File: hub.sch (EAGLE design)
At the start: 51 parts, among them U1 LM3526-L, X1 12MHz

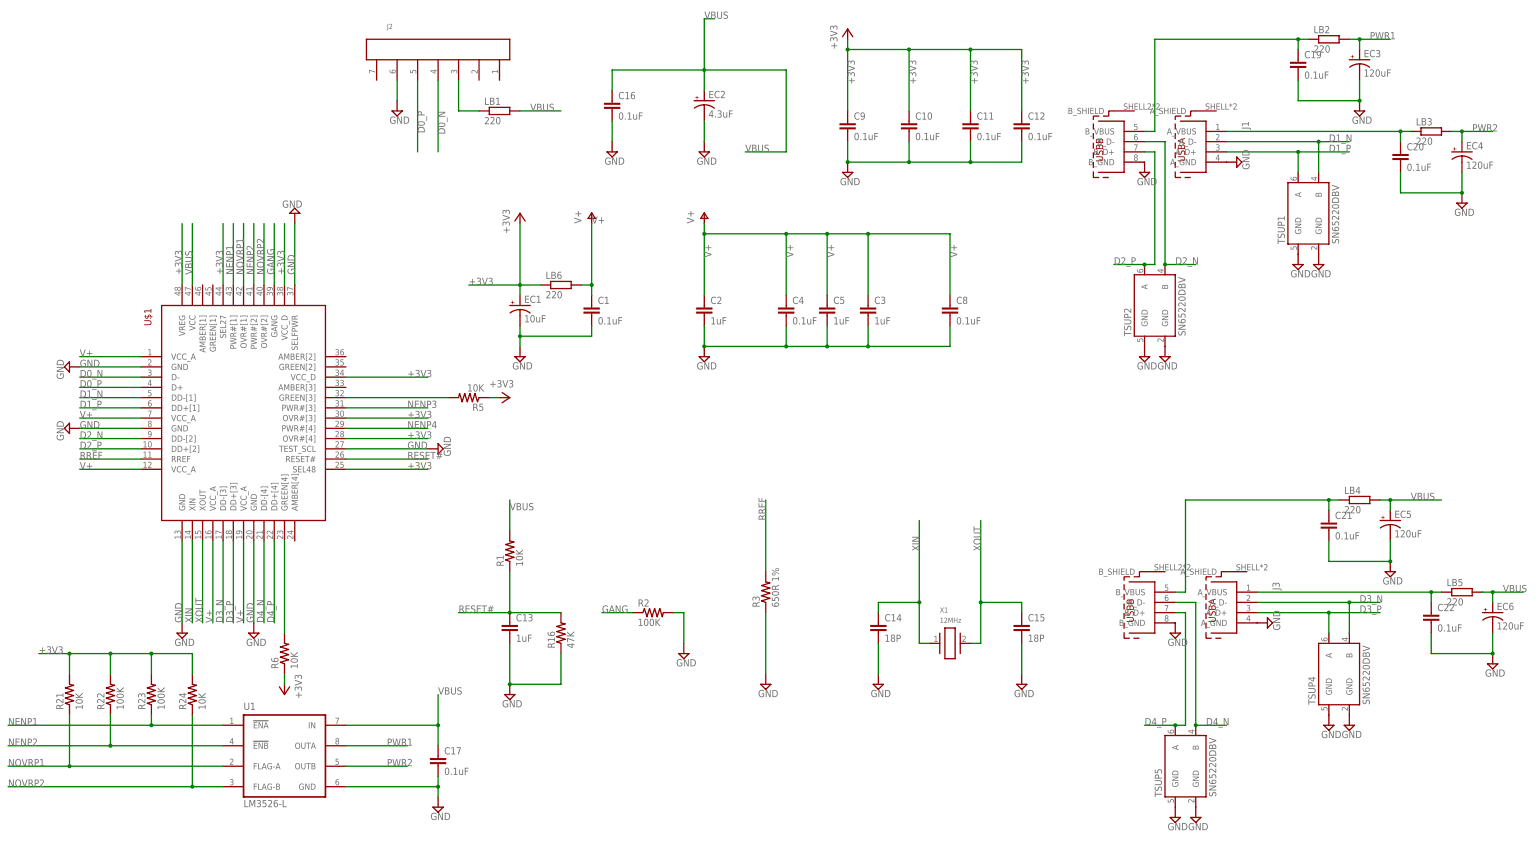
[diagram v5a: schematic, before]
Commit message: finish silk screen
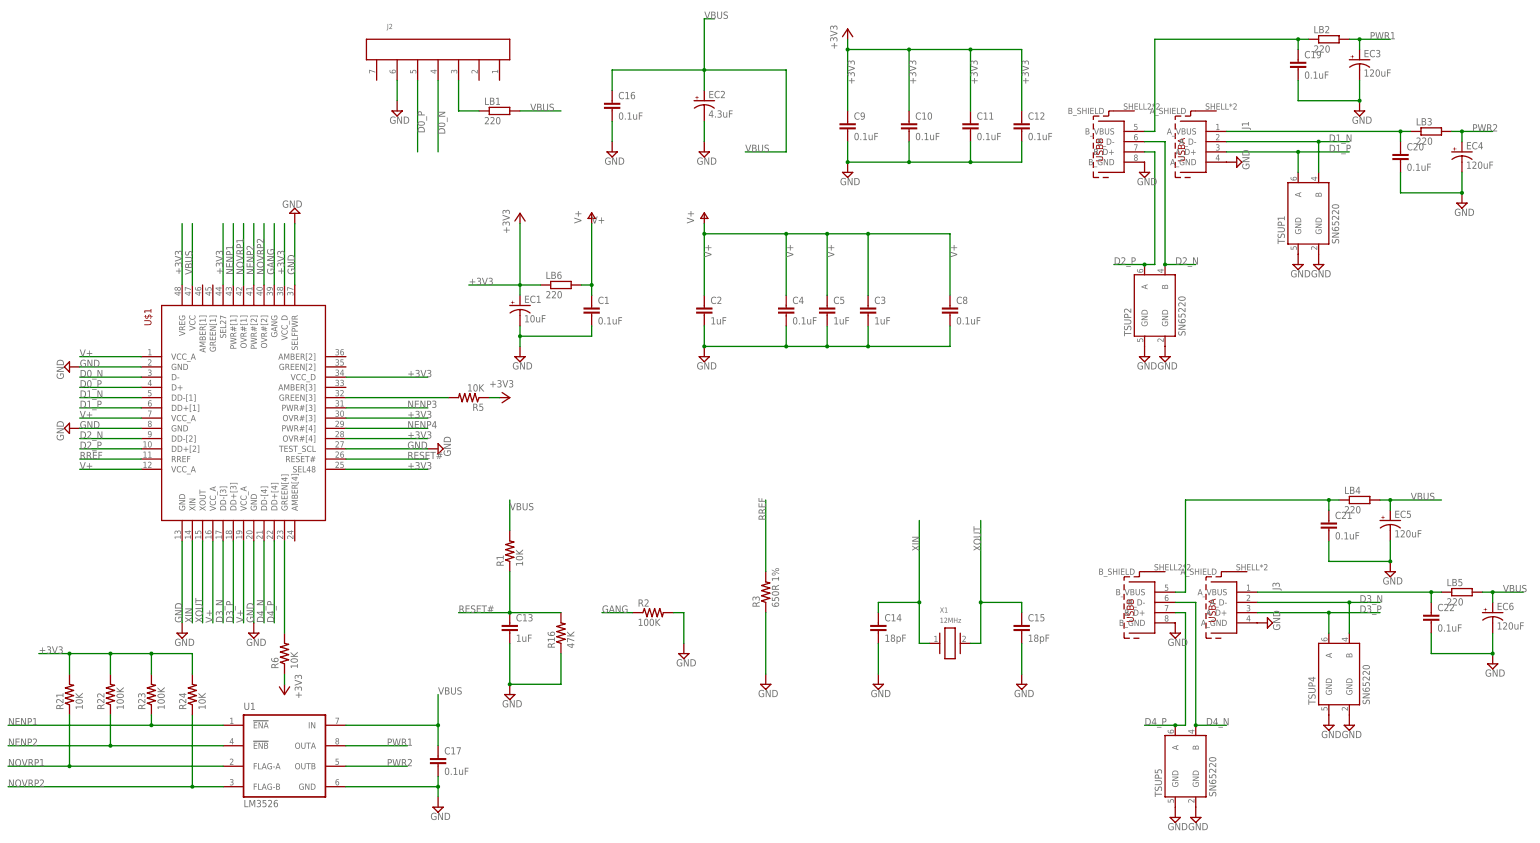
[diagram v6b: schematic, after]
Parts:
- C14, C15: value 18P -> 18pF
- TSUP1, TSUP2, TSUP4, TSUP5: value SN65220DBV -> SN65220
- U$1: value CY7C65634-48AXCT -> CY7C65632; DIGIKEY 428-3153-1-ND -> 428-3155-1-ND; MPN CY7C65634-48AXCT -> CY7C65632-48AXCT; OC_MOUSER 727-CY7C65634-48AXCT -> 727-CY7C65632-48AXCT
- U1: value LM3526-L -> LM3526
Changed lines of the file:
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@@
 <attribute name="OC_MOUSER" value="571-440054-7"/>
 </part>
-<part name="U$1" library="CY7C65634-48AXCT" deviceset="CY7C65634-48AXCT" device="">
-<attribute name="DIGIKEY" value="428-3153-1-ND"/>
-<attribute name="MPN" value="CY7C65634-48AXCT"/>
-<attribute name="OC_MOUSER" value="727-CY7C65634-48AXCT"/>
+<part name="U$1" library="CY7C65634-48AXCT" deviceset="CY7C65634-48AXCT" device="" value="CY7C65632">
+<attribute name="DIGIKEY" value="428-3155-1-ND"/>
+<attribute name="MPN" value="CY7C65632-48AXCT"/>
+<attribute name="OC_MOUSER" value="727-CY7C65632-48AXCT"/>
 </part>
 <part name="SUPPLY1" library="supply2" library_urn="urn:adsk.eagle:library:372" deviceset="GND" device=""/>
@@
 </part>
 <part name="SUPPLY4" library="supply2" library_urn="urn:adsk.eagle:library:372" deviceset="GND" device=""/>
-<part name="C14" library="rcl" library_urn="urn:adsk.eagle:library:334" deviceset="C-EU" device="C0805" package3d_urn="urn:adsk.eagle:package:23617/2" value="18P">
+<part name="C14" library="rcl" library_urn="urn:adsk.eagle:library:334" deviceset="C-EU" device="C0805" package3d_urn="urn:adsk.eagle:package:23617/2" value="18pF">
 <attribute name="DIGIKEY" value="1276-1089-1-ND"/>
 <attribute name="MPN" value="CL10C180JB8NNNC"/>
 <attribute name="OC_MOUSER" value="77-VJ0603A180JXACBC"/>
 </part>
-<part name="C15" library="rcl" library_urn="urn:adsk.eagle:library:334" deviceset="C-EU" device="C0805" package3d_urn="urn:adsk.eagle:package:23617/2" value="18P">
+<part name="C15" library="rcl" library_urn="urn:adsk.eagle:library:334" deviceset="C-EU" device="C0805" package3d_urn="urn:adsk.eagle:package:23617/2" value="18pF">
 <attribute name="DIGIKEY" value="1276-1089-1-ND"/>
 <attribute name="MPN" value="CL10C180JB8NNNC"/>
@@
 <part name="SUPPLY9" library="supply2" library_urn="urn:adsk.eagle:library:372" deviceset="GND" device=""/>
 <part name="SUPPLY10" library="supply2" library_urn="urn:adsk.eagle:library:372" deviceset="GND" device=""/>
-<part name="TSUP1" library="sn65220_40" deviceset="SN65220" device="DBV">
+<part name="TSUP1" library="sn65220_40" deviceset="SN65220" device="DBV" value="SN65220">
 <attribute name="DIGIKEY" value="296-9694-1-ND"/>
 <attribute name="MPN" value="SN65220DBVR"/>
@@
 <attribute name="OC_MOUSER" value="81-BLM21P221SG"/>
 </part>
-<part name="TSUP2" library="sn65220_40" deviceset="SN65220" device="DBV">
+<part name="TSUP2" library="sn65220_40" deviceset="SN65220" device="DBV" value="SN65220">
 <attribute name="DIGIKEY" value="296-9694-1-ND"/>
 <attribute name="MPN" value="SN65220DBVR"/>
@@
 </part>
 <part name="SUPPLY19" library="supply2" library_urn="urn:adsk.eagle:library:372" deviceset="GND" device=""/>
-<part name="U1" library="national-semi" deviceset="LM3526-L" device="">
+<part name="U1" library="national-semi" deviceset="LM3526-L" device="" value="LM3526">
 <attribute name="DIGIKEY" value="LM3526MX-L/NOPBCT-ND"/>
 <attribute name="MPN" value="LM3526MX-L/NOPB"/>
@@
 <attribute name="OC_MOUSER" value="81-BLM21P221SG"/>
 </part>
-<part name="TSUP4" library="sn65220_40" deviceset="SN65220" device="DBV">
+<part name="TSUP4" library="sn65220_40" deviceset="SN65220" device="DBV" value="SN65220">
 <attribute name="DIGIKEY" value="296-9694-1-ND"/>
 <attribute name="MPN" value="SN65220DBVR"/>
@@
 <attribute name="OC_MOUSER" value="81-BLM21P221SG"/>
 </part>
-<part name="TSUP5" library="sn65220_40" deviceset="SN65220" device="DBV">
-<attribute name="DIGIKEY" value="296-9694-1-ND"/>
-<attribute name="MPN" value="SN65220DBVR"/>
+<part name="TSUP5" library="sn65220_40" deviceset="SN65220" device="DBV" value="SN65220">
+<attribute name="DIGIKEY" value="296-9694-1-ND"/>
+<attribute name="MPN" value="SN65220DBVR"/>
